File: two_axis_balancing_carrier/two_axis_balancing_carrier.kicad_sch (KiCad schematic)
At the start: 0 parts

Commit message: Power board topology finished and carrier board started
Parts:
- added C1, C2: C, symbol Device:C
- added J1: Conn_01x03, symbol Connector_Generic:Conn_01x03
- added J5: Conn_02x05, symbol Connector_Generic:Conn_02x05_Odd_Even
- added U1: NUCLEO-G474RE, NUCLEO-G474RE:MODULE_NUCLEO-G474RE, symbol NUCLEO-G474RE:NUCLEO-G474RE
- added U2: MIC5219-3.3YM5, Package_TO_SOT_SMD:SOT-23-5, symbol Regulator_Linear:MIC5219-3.3YM5
- added U3: ICM-42688-P, LGA14_2P5X3X0P91_TDK, symbol 2026-06-02_00-25-06:ICM-42688-P
- added U4: SN65HVD230, Package_SO:SOIC-8_3.9x4.9mm_P1.27mm, symbol Interface_CAN_LIN:SN65HVD230
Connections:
- new net: C1.1, U2.4 (BP)
- new net +3.3V: C2.1, U2.5 (OUT), U3.5 (VDDIO), U3.8 (VDD), U4.3 (VCC)
- new net +5V: J5.1 (Pin_1), U2.1 (IN), U2.3 (EN)
- new net AIN1: J5.5 (Pin_5)
- new net BAT_LEV: J5.3 (Pin_3)
- new net BAT_LOW: J5.4 (Pin_4)
- new net CANH: J1.1 (Pin_1), U4.7 (CANH)
- new net CANL: J1.2 (Pin_2), U4.6 (CANL)
- new net CS: U3.12 (AP_CS)
- new net GND: C1.2, C2.2, J1.3 (Pin_3), J5.10 (Pin_10), J5.2 (Pin_2), J5.6 (Pin_6), U2.2 (GND), U3.10 (RESV), U3.11 (RESV), U3.2 (RESV), U3.3 (RESV), U3.6 (GND), U3.7 (RESV), U4.2 (GND), U4.8 (Rs)
- new net INT1: U3.4 (INT1/INT)
- new net INT2: U3.9 (INT2/FSYNC/CLKIN)
- new net PWMA: J5.8 (Pin_8)
- new net RX: U4.4 (R)
- new net SCLK: U3.13 (AP_SCL/AP_SCLK)
- new net SDI: U3.14 (AP_SDA/AP_SDIO/AP_SDI)
- new net SDO: U3.1 (AP_SDO/AP_AD0)
- new net STBY: J5.9 (Pin_9)
- new net TX: U4.1 (D)
- no-connect marks 0 -> 1

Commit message: Finished topology
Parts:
- added C3, C4, C5: C, symbol Device:C
- added J2: Conn_01x04, symbol Connector_Generic:Conn_01x04
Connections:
- net +3.3V: now also C3.1, C4.2, C5.2
- net +5V: now also J2.1 (Pin_1)
- net AIN2: now also J5.7 (Pin_7)
- net GND: now also C3.2, C4.1, C5.1, J2.4 (Pin_4)
- new net ENC_A: J2.2 (Pin_2)
- new net ENC_B: J2.3 (Pin_3)
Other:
- moved on the sheet: C1, C2, J1, J5, U1A, U1B, U2, U3, U4

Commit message: Sized passives
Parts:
- added C6: 2.2uF, symbol Device:C
- added R1, R2: 120R, symbol Device:R_US
- C1: value C -> 470pF
- C2: value C -> 2.2uF
- C3, C5: value C -> 100nF
- C4: value C -> 10nF
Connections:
- net +3.3V: now also C5.1, C6.1; no longer C5.2
- net CANH: now also R1.1, R2.1
- net CANL: now also R1.2, R2.2
- net GND: now also C5.2, C6.2; no longer C5.1
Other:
- moved on the sheet: C2, C3, C5

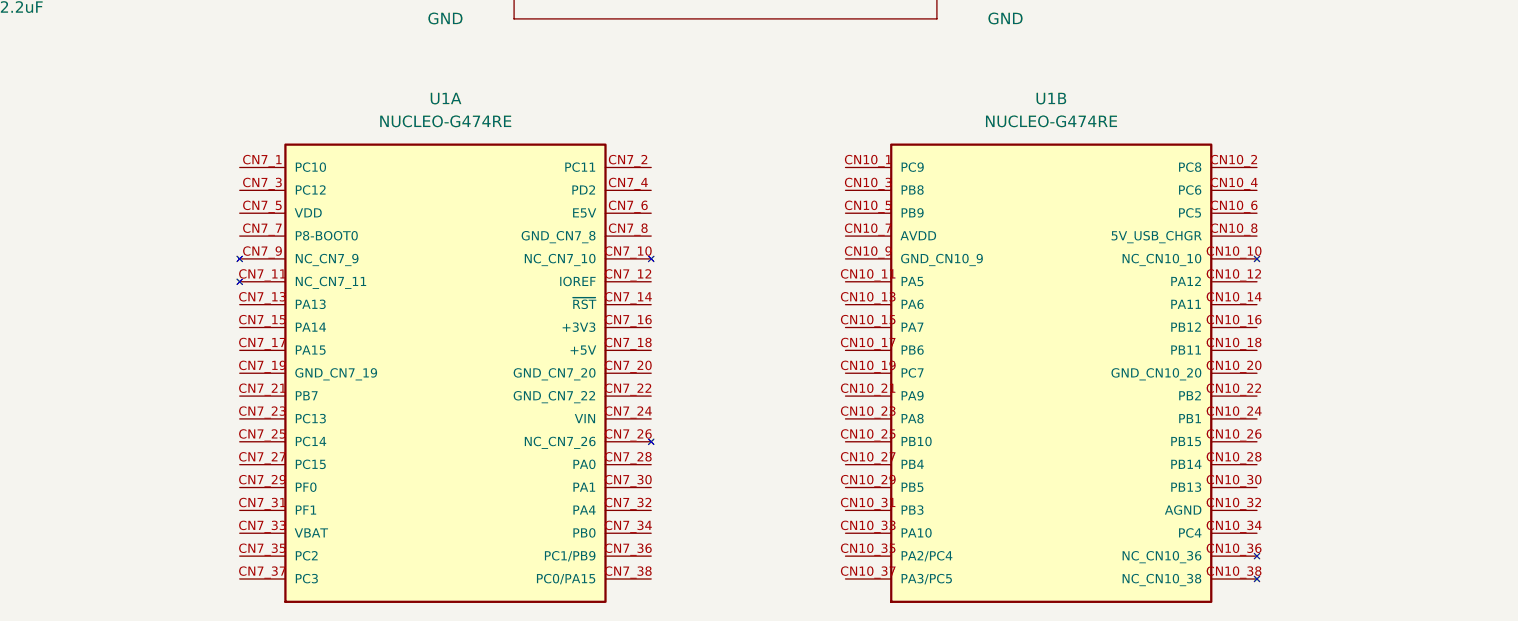
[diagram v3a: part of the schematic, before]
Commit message: Carrier schematic finished and power board polished
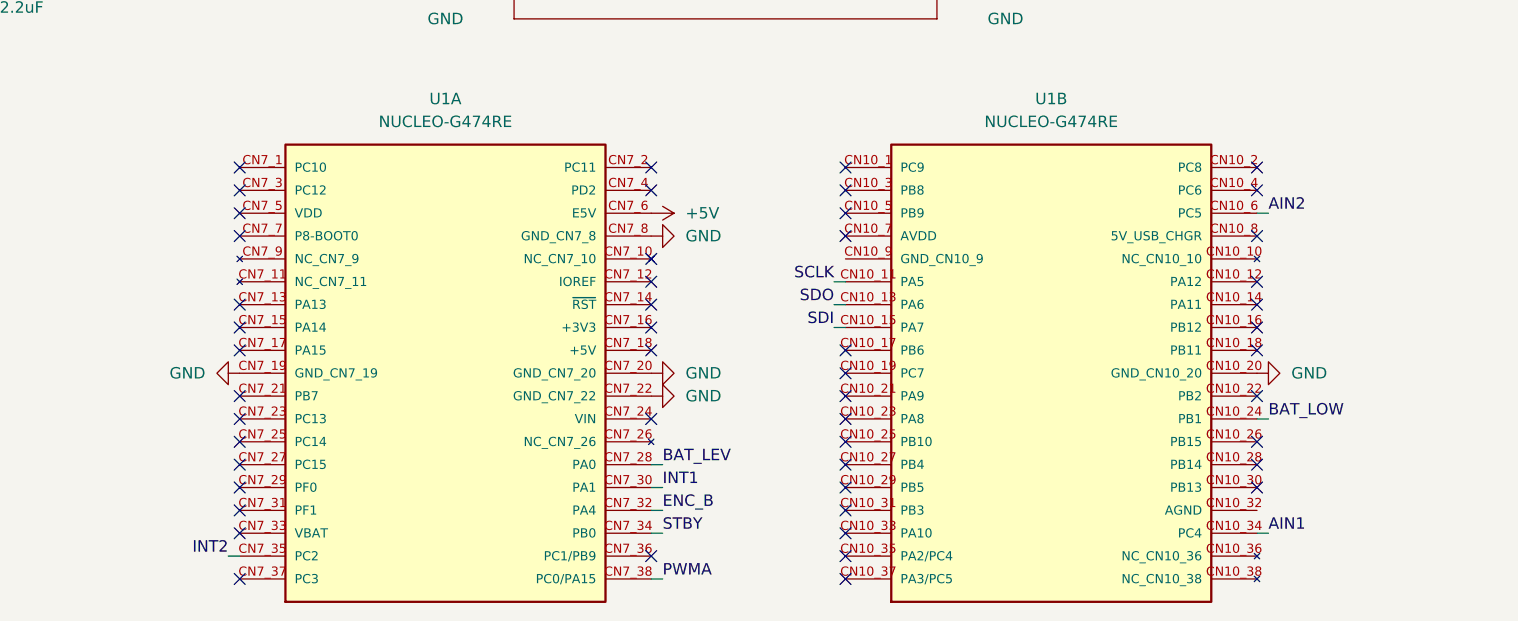
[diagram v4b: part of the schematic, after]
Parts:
- C1, C3, C4, C5: footprint (none) -> Capacitor_SMD:C_0603_1608Metric
- C2, C6: footprint (none) -> Capacitor_SMD:C_0805_2012Metric
- J1: footprint (none) -> Connector_PinSocket_2.54mm:PinSocket_1x03_P2.54mm_Vertical
- J2: footprint (none) -> Connector_PinSocket_2.54mm:PinSocket_1x04_P2.54mm_Vertical
- J5: footprint (none) -> Connector_IDC:IDC-Header_2x05_P2.54mm_Vertical
- R1, R2: footprint (none) -> Resistor_SMD:R_0603_1608Metric
- U1: footprint NUCLEO-G474RE:MODULE_NUCLEO-G474RE -> NUCLEO-G474:MODULE_NUCLEO-G474RE
- U3: footprint LGA14_2P5X3X0P91_TDK -> ICM:LGA14_2P5X3X0P91_TDK
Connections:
- net +5V: now also U1.CN7_6 (E5V)
- net AIN1: now also U1.CN10_34 (PC4)
- net AIN2: now also U1.CN10_6 (PC5)
- net BAT_LEV: now also U1.CN7_28 (PA0)
- net BAT_LOW: now also U1.CN10_24 (PB1)
- net ENC_B: now also U1.CN7_32 (PA4)
- net GND: now also U1.CN10_20 (GND_CN10_20), U1.CN7_19 (GND_CN7_19), U1.CN7_20 (GND_CN7_20), U1.CN7_22 (GND_CN7_22), U1.CN7_8 (GND_CN7_8)
- net INT1: now also U1.CN7_30 (PA1)
- net INT2: now also U1.CN7_35 (PC2)
- net PWMA: now also U1.CN7_38 (PC0/PA15)
- net SCLK: now also U1.CN10_11 (PA5)
- net SDI: now also U1.CN10_15 (PA7)
- net SDO: now also U1.CN10_13 (PA6)
- net STBY: now also U1.CN7_34 (PB0)
- no-connect marks 1 -> 51

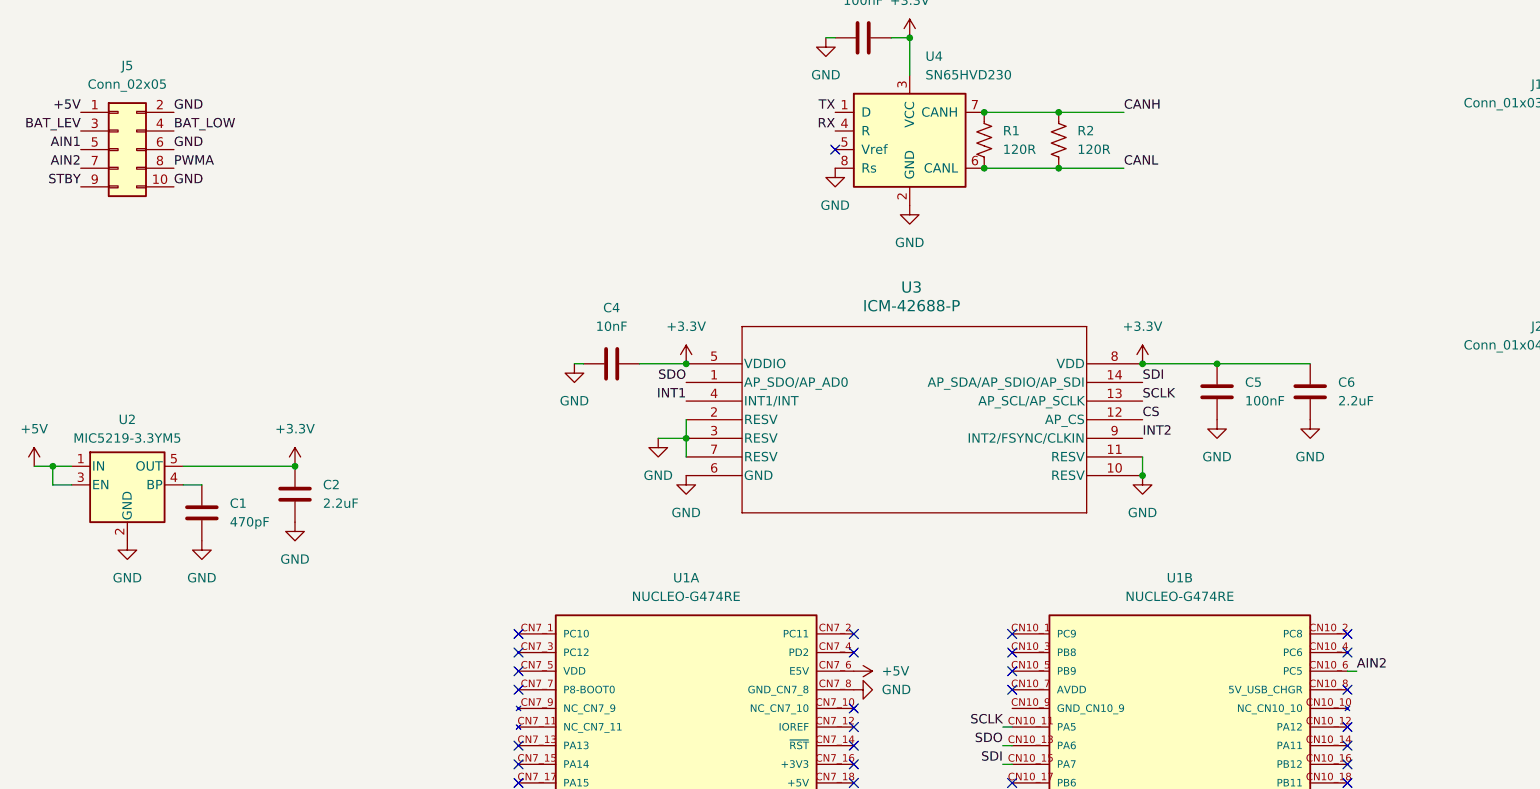
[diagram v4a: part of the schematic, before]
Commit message: Power actually finished; carrier pcb started
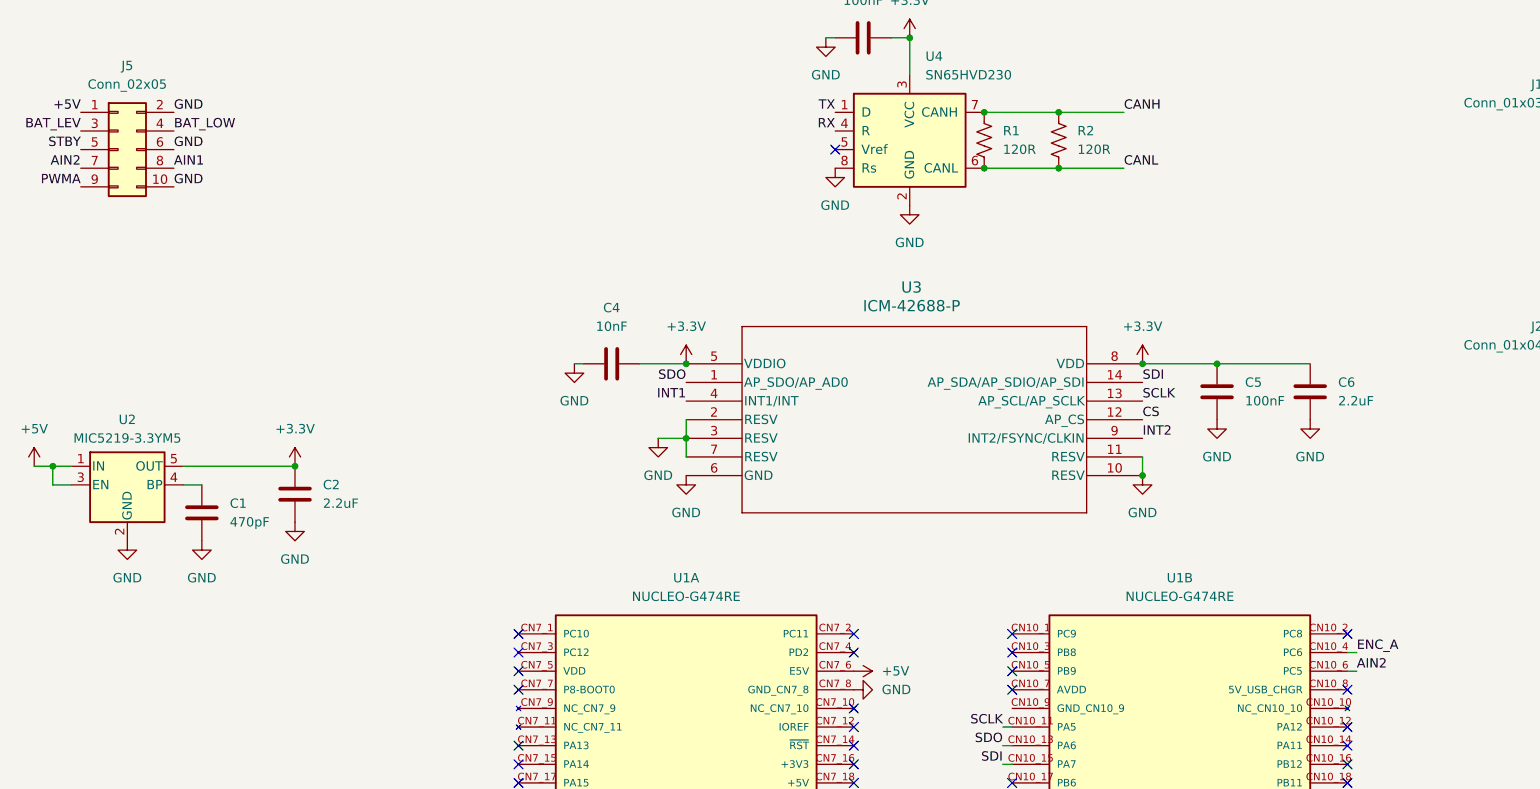
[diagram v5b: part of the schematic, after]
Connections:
- net AIN1: now also J5.8 (Pin_8); no longer J5.5 (Pin_5)
- net ENC_A: now also U1.CN10_4 (PC6)
- net PWMA: now also J5.9 (Pin_9); no longer J5.8 (Pin_8)
- net STBY: now also J5.5 (Pin_5); no longer J5.9 (Pin_9)
- no-connect marks 51 -> 50
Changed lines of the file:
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@@
-	)
-	(no_connect
-		(at 219.71 114.3)
 	)
 	(no_connect
@@
 	(wire
 		(pts
+			(xy 220.98 114.3) (xy 219.71 114.3)
+		)
+		(stroke
+			(width 0)
+			(type default)
+		)
+	)
+	(wire
+		(pts
 			(xy 129.54 85.09) (xy 129.54 87.63)
 		)
@@
 	)
 	(label "AIN1"
-		(at 46.99 45.72 180)
-		(effects
-			(font
-				(size 1.27 1.27)
-			)
-			(justify right bottom)
+		(at 59.69 48.26 0)
+		(effects
+			(font
+				(size 1.27 1.27)
+			)
+			(justify left bottom)
 		)
 	)
@@
 	)
 	(label "STBY"
-		(at 46.99 50.8 180)
+		(at 46.99 45.72 180)
 		(effects
 			(font
@@
 		)
 	)
+	(label "ENC_A"
+		(at 220.98 114.3 0)
+		(effects
+			(font
+				(size 1.27 1.27)
+			)
+			(justify left bottom)
+		)
+	)
 	(label "BAT_LOW"
 		(at 220.98 139.7 0)
@@
 	)
 	(label "PWMA"
-		(at 59.69 48.26 0)
-		(effects
-			(font
-				(size 1.27 1.27)
-			)
-			(justify left bottom)
-		)
-	)
+		(at 46.99 50.8 180)
+		(effects
+			(font
+				(size 1.27 1.27)
+			)
+			(justify right bottom)
+		)
+	)

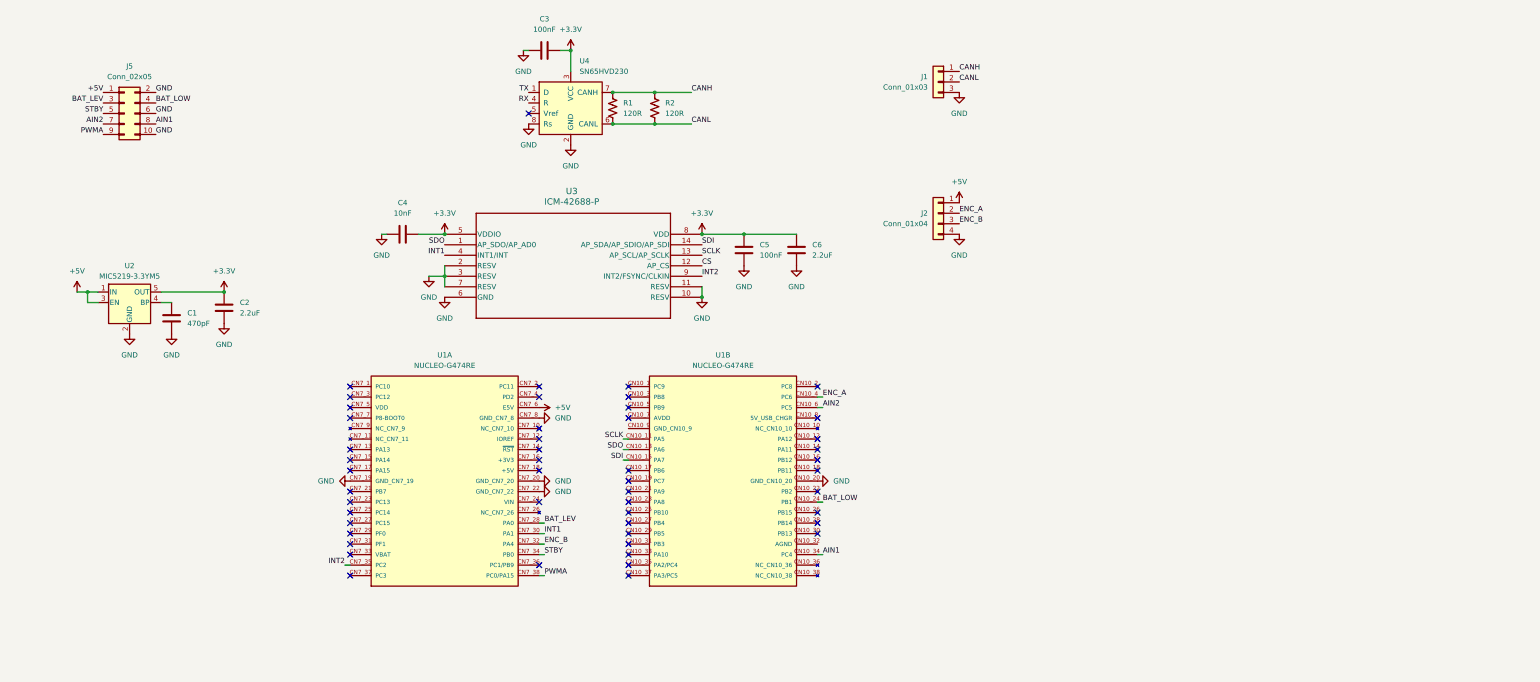
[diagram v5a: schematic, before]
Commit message: Carrier layout finished
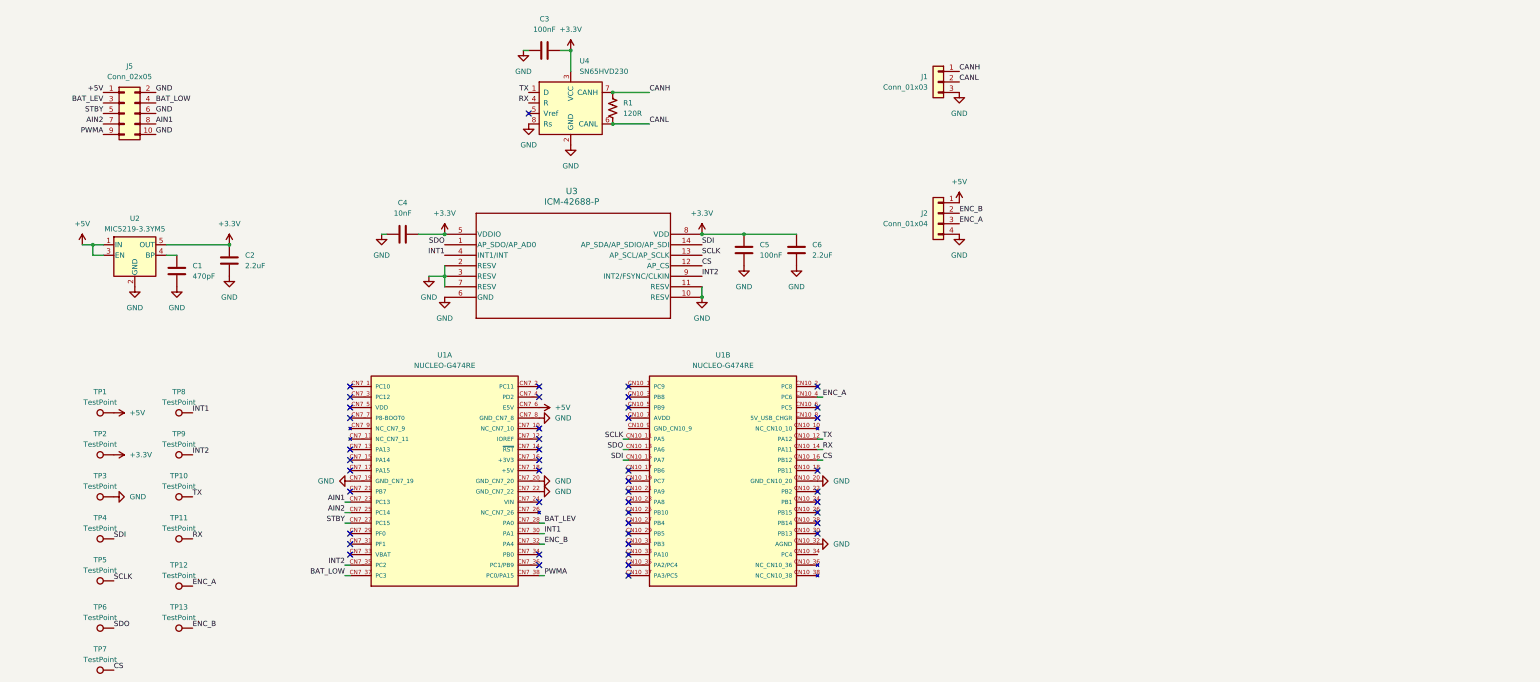
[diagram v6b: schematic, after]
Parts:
- removed R2: 120R, Resistor_SMD:R_0603_1608Metric, symbol Device:R_US
- added TP1, TP10, TP11, TP12, TP13, TP2, TP3, TP4, TP5, TP6, TP7, TP8, TP9: TestPoint, TestPoint:TestPoint_Pad_2.0x2.0mm, symbol Connector:TestPoint
- J1: footprint Connector_PinSocket_2.54mm:PinSocket_1x03_P2.54mm_Vertical -> Connector_JST:JST_XH_B3B-XH-A_1x03_P2.50mm_Vertical
- J2: footprint Connector_PinSocket_2.54mm:PinSocket_1x04_P2.54mm_Vertical -> Connector_JST:JST_XH_B4B-XH-A_1x04_P2.50mm_Vertical
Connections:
- net +3.3V: now also TP2.1
- net +5V: now also TP1.1
- net AIN1: now also U1.CN7_23 (PC13); no longer U1.CN10_34 (PC4)
- net AIN2: now also U1.CN7_25 (PC14); no longer U1.CN10_6 (PC5)
- net BAT_LOW: now also U1.CN7_37 (PC3); no longer U1.CN10_24 (PB1)
- net CS: now also U1.CN10_16 (PB12), TP7.1
- net ENC_A: now also J2.3 (Pin_3), TP12.1; no longer J2.2 (Pin_2)
- net ENC_B: now also J2.2 (Pin_2), TP13.1; no longer J2.3 (Pin_3)
- net GND: now also U1.CN10_32 (AGND), TP3.1
- net INT1: now also TP8.1
- net INT2: now also TP9.1
- net RX: now also U1.CN10_14 (PA11), TP11.1
- net SCLK: now also TP5.1
- net SDI: now also TP4.1
- net SDO: now also TP6.1
- net STBY: now also U1.CN7_27 (PC15); no longer U1.CN7_34 (PB0)
- net TX: now also U1.CN10_12 (PA12), TP10.1
- no-connect marks 50 -> 46
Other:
- moved on the sheet: C1, C2, U2
